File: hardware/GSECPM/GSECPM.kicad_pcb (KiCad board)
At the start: 2 copper layers, 167.8 x 110.5 mm, 67 parts, among them J1 N2-Bottle PT, J10 Ignition E-Match, J11 QD E-Match, J12 Radio Module Connector, J13 Purge Servo, J14 Power Input, J15 Internal Cooling, J16 Nitrous Cooling, J17 Load Cell + Amp, J2 K-Bottle TC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

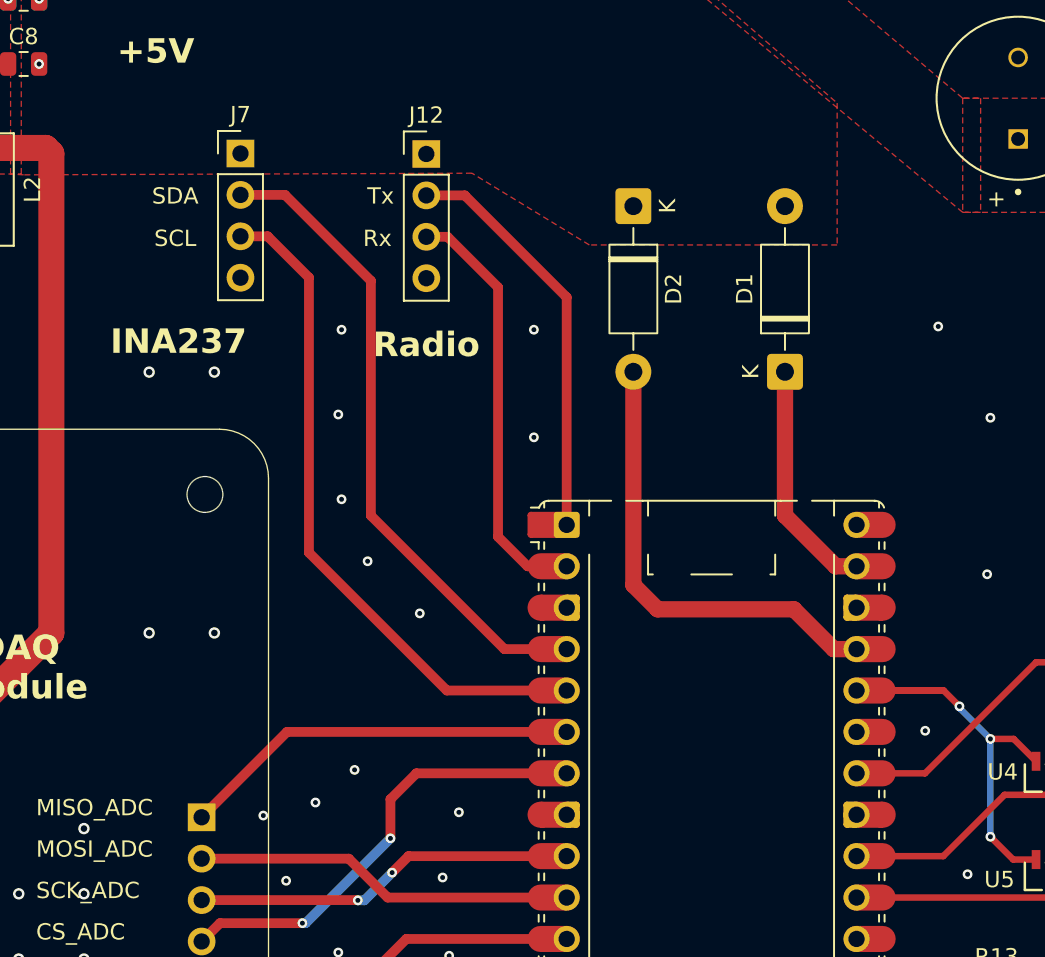
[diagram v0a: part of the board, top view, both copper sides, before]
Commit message: Swapped positions of radio and INA237 conns for optimized current loop. Swapped 9V LDO to a TI model that supports newer ceramic caps better than the original STM legacy LDO
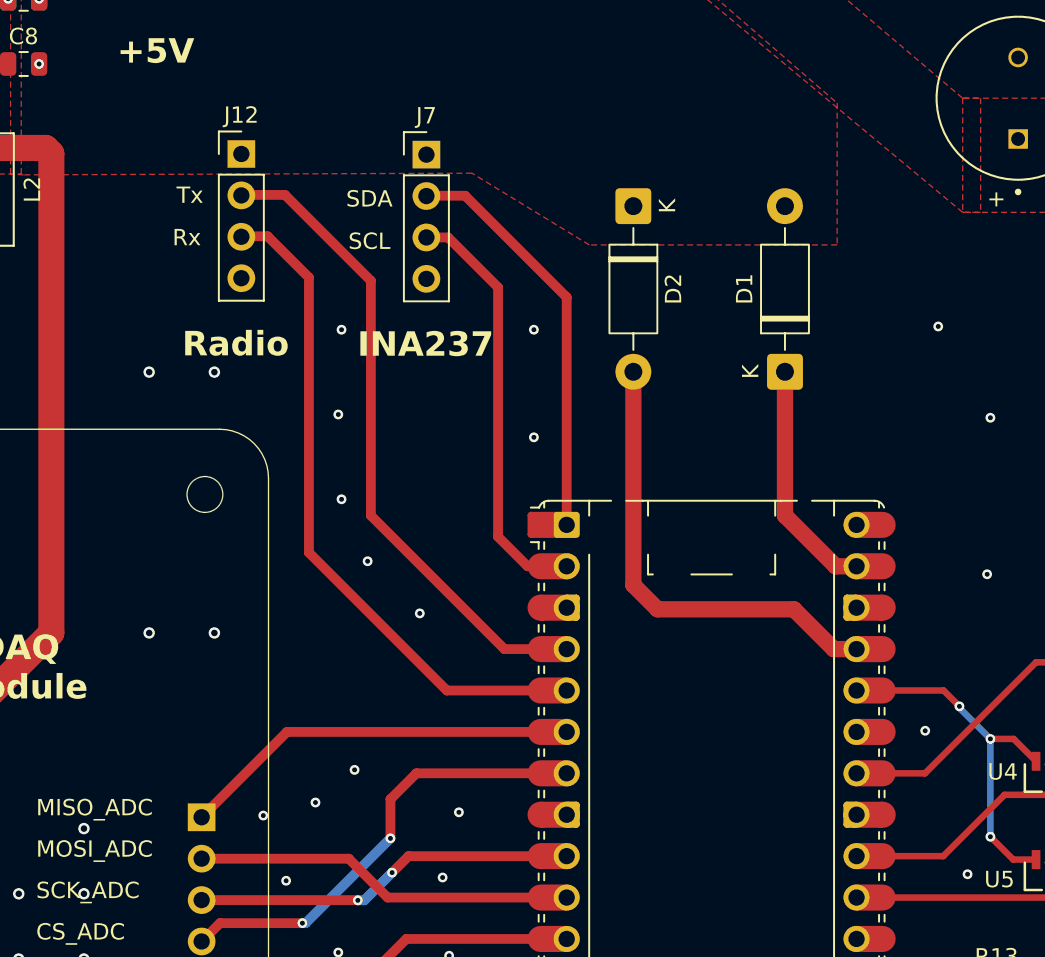
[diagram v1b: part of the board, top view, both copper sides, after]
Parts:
- U1: value L78M09CDT-TR -> UA78M09CKVURG3
- moved J7 11.4 mm to (139.7, 51.1)
- moved J12 11.3 mm to (128.3, 51.1)
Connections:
- A1 pad 1: /GPIO0 (Radio_UART_TX) -> /GPIO0_INA237 SDA
- A1 pad 2: /GPIO1 (Radio_UART_RX) -> /GPIO1_INA237 SCL
- A1 pad 4: /GPIO2_INA237 SDA -> /GPIO2 (Radio_UART_TX)
- A1 pad 5: /GPIO3_INA237 SCL -> /GPIO3 (Radio_UART_RX)
- J12 pad 2: /GPIO0 (Radio_UART_TX) -> /GPIO2 (Radio_UART_TX)
- J12 pad 3: /GPIO1 (Radio_UART_RX) -> /GPIO3 (Radio_UART_RX)
- J7 pad 2: /GPIO2_INA237 SDA -> /GPIO0_INA237 SDA
- J7 pad 3: /GPIO3_INA237 SCL -> /GPIO1_INA237 SCL
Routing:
- net /GPIO3_INA237 SCL: track 41.4 -> 0.00 mm
- net /GPIO3 (Radio_UART_RX): track 0.00 -> 41.4 mm
- net /GPIO2 (Radio_UART_TX): track 0.00 -> 40.8 mm
- net /GPIO2_INA237 SDA: track 40.0 -> 0.00 mm
- net /GPIO1_INA237 SCL: track 0.00 -> 25.9 mm
- net /GPIO1 (Radio_UART_RX): track 25.9 -> 0.00 mm
- net /GPIO0 (Radio_UART_TX): track 25.2 -> 0.00 mm
- net /GPIO0_INA237 SDA: track 0.00 -> 25.2 mm
- net +3.3V: track 26.8 -> 22.2 mm
- net Net-(A1-GPIO27_ADC1): track 17.8 -> 18.6 mm

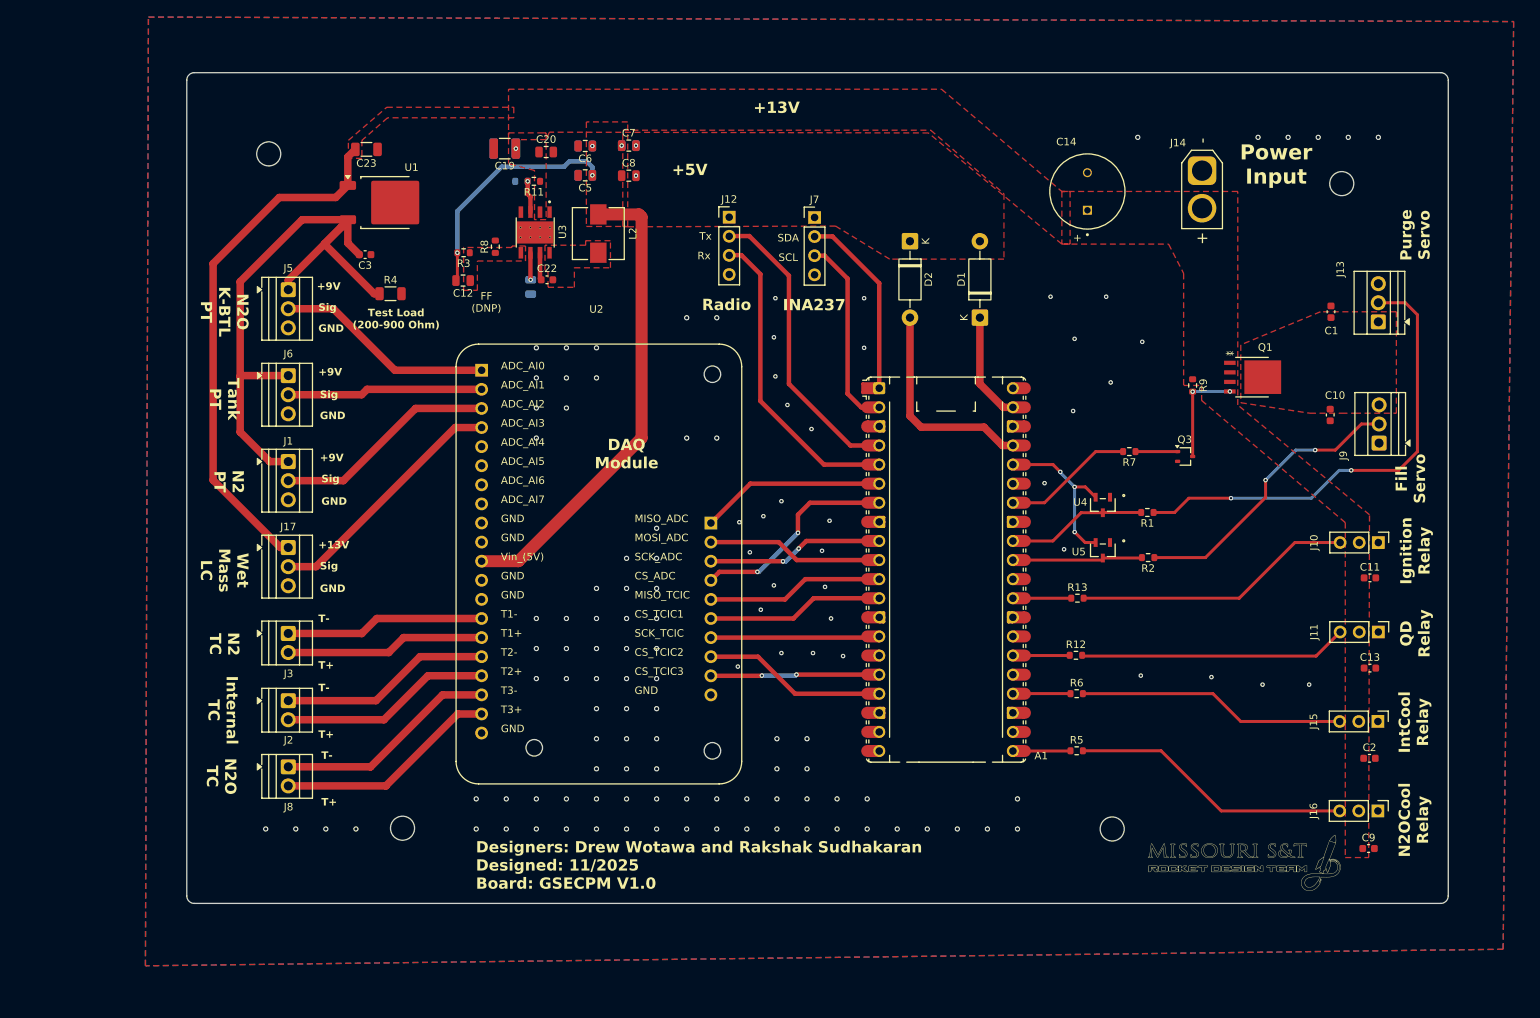
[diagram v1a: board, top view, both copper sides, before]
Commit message: Made all buck components on front layer
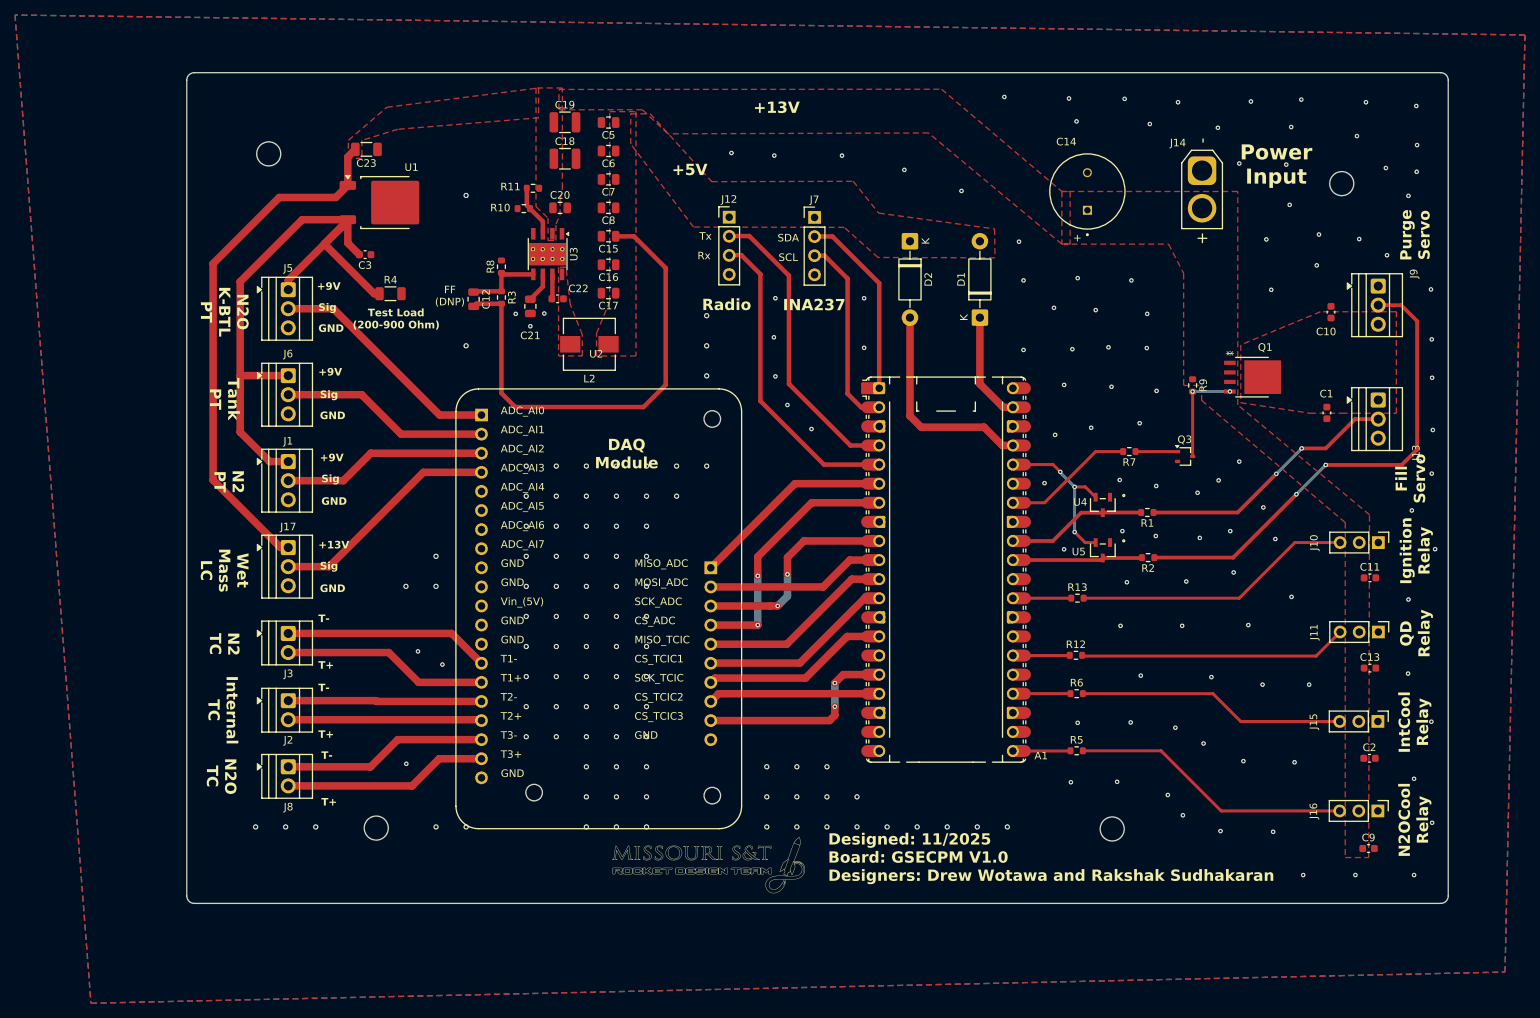
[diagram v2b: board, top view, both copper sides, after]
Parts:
- C15, C16, C17, C18, C21, R10: moved to F.Cu
- U3: footprint LMR33640ADDAR:VREG_LM5017MR_NOPB -> Package_SO:Texas_HSOP-8-1EP_3.9x4.9mm_P1.27mm_ThermalVias
- moved G*** 71.3 mm to (125.5, 137.3)
- moved J9 20.9 mm to (214.6, 60.3), turned to -90 degrees
- moved C17 19.8 mm to (112.2, 61.2), turned to 180 degrees
- moved C16 16.1 mm to (112.2, 57.4)
- moved L2 14.8 mm to (109.7, 68.0), turned to 0 degrees
- moved C10 13.7 mm to (208.3, 63.7), turned to 90 degrees
- moved C1 13.5 mm to (207.8, 77.1), turned to 90 degrees
- moved J13 10.4 mm to (214.6, 75.4), turned to -90 degrees
- moved C19 8.74 mm to (106.5, 38.5), turned to 0 degrees
- moved C15 8.69 mm to (112.2, 53.6)
- moved C18 8.12 mm to (106.5, 43.3), turned to 0 degrees
- moved R3 7.80 mm to (98.0, 61.8), turned to -90 degrees
- moved C5 7.67 mm to (112.2, 38.5)
- moved C20 7.66 mm to (105.8, 49.9)
- moved U2 5.96 mm to (110.6, 69.8)
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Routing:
- net +5V: track 94.8 -> 63.5 mm, vias 4 -> 0
- net /GPIO27 (Purge Servo): track 62.5 -> 35.0 mm
- net /GPIO26 (Fill Servo): track 38.6 -> 64.0 mm
- net /BuckConverter/FB: track 0.00 -> 10.5 mm
- net /GPIO5 (CS_ADC): track 28.1 -> 34.5 mm
- net /GPIO6 (SCK_ADC): track 23.5 -> 29.0 mm
- net /GPIO12 (CS_N2O): track 22.5 -> 27.5 mm
- net /GPIO10 (SCK_TCIC): track 22.5 -> 25.2 mm
- net Net-(U3-EN): track 4.25 -> 6.94 mm, vias 1 -> 0
- net /T+ (N2O): track 29.7 -> 27.2 mm
- net /T- (N2O): track 29.7 -> 27.2 mm
- net /GPIO9 (CS_N2): track 23.5 -> 26.0 mm
- net /ADC_AI3: track 33.4 -> 30.9 mm
- net /GPIO4 (MISO_ADC): track 24.6 -> 27.0 mm
- net /GPIO8 (MISO_TCIC): track 23.5 -> 26.0 mm
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- removed copper zone on F.Cu, net /BuckConverter/FB
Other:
- board text added: "Designed: 11/2025 Board: GSECPM V1.0 Designers: Drew Wotawa and Rakshak Sudhakaran"
- board text added: "{ "ViaStitching": "0.2", "stitch_zone_0": { "HSpacing": "1", "VSpacing": "1", "HOffset": "0", "VOffset": "0", "Clearance": "1", "Randomize": false } }"
- board text added: "{ "ViaStitching": "0.2", "stitch_zone_0": { "HSpacing": "4", "VSpacing": "4", "HOffset": "0", "VOffset": "0", "Clearance": "0", "Randomize": false } }"
- board text removed: "Designers: Drew Wotawa and Rakshak Sudhakaran Designed: 11/2025 Board: GSECPM V1.0"

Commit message: Better buck converter positioning with inductor further from analog signals. Improved via stitching and fixed split ground planes somewhat except for Manhattans
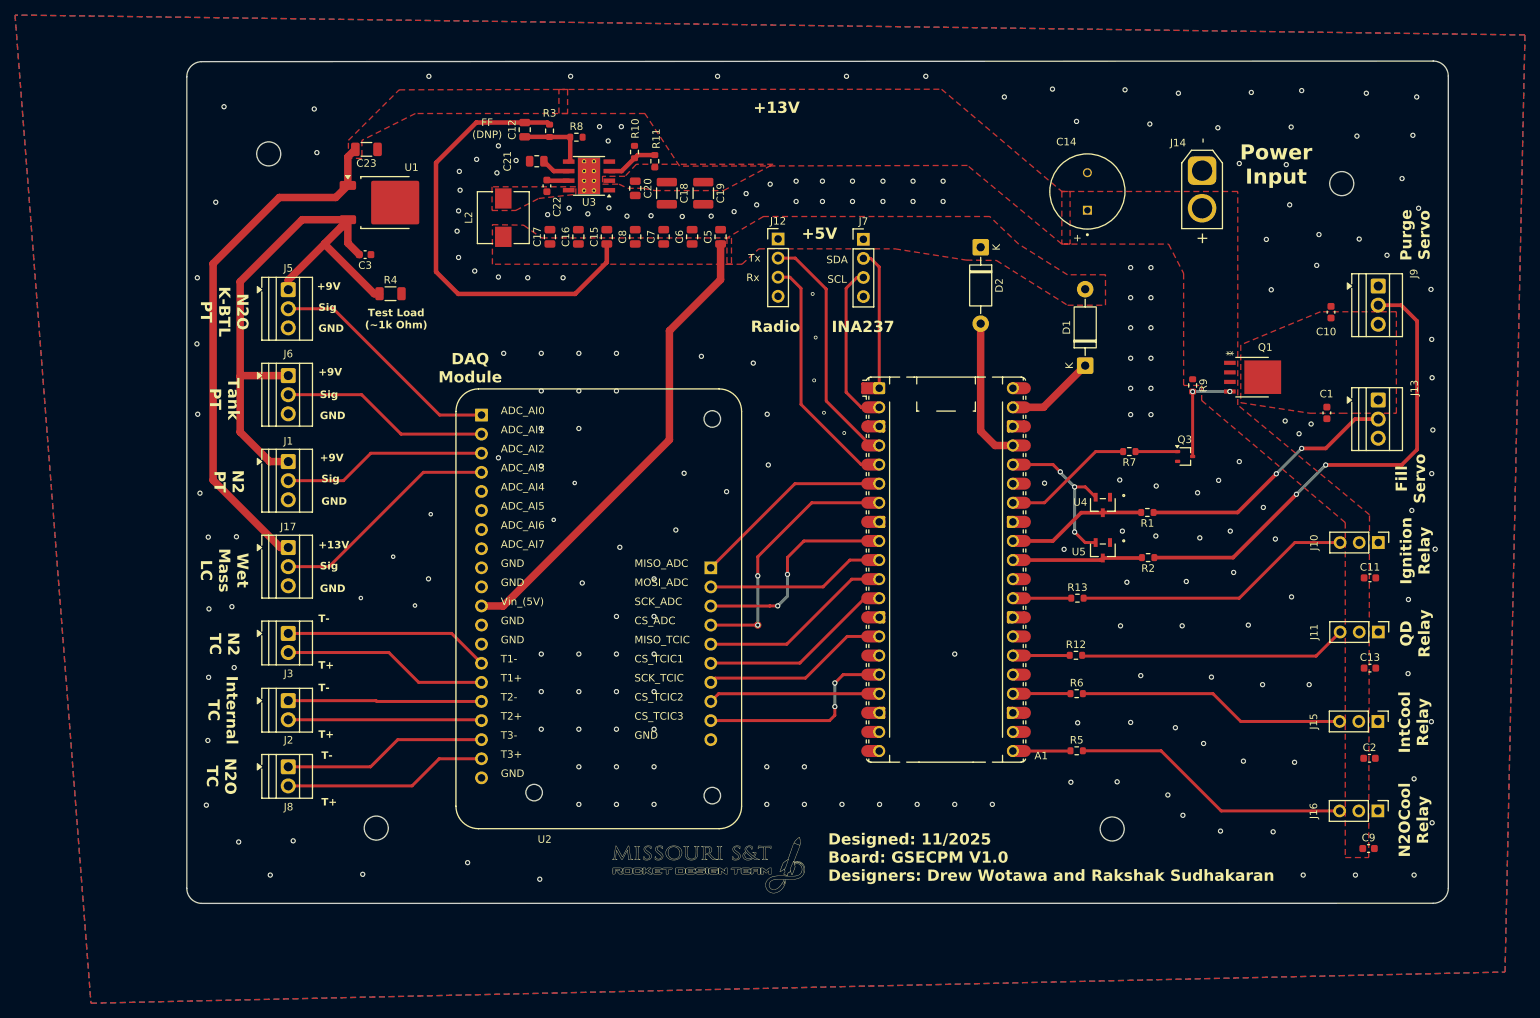
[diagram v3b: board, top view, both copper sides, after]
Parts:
- moved C12 23.6 mm to (101.1, 39.5), turned to 90 degrees
- moved R3 23.1 mm to (104.4, 39.6), turned to 90 degrees
- moved C5 21.3 mm to (127.2, 53.7), turned to 90 degrees
- moved C19 20.7 mm to (124.8, 47.9), turned to -90 degrees
- moved L2 20.4 mm to (98.2, 51.1), turned to -90 degrees
- moved R8 19.9 mm to (108.0, 40.5), turned to 0 degrees
- moved C21 19.3 mm to (102.7, 43.6), turned to 180 degrees
- moved R11 16.6 mm to (118.4, 43.6), turned to 90 degrees
- moved R10 16.5 mm to (115.7, 42.4), turned to -90 degrees
- moved C6 15.9 mm to (123.4, 53.7), turned to 90 degrees
- moved D1 15.4 mm to (175.7, 70.8)
- moved C22 15.1 mm to (104.0, 46.9), turned to -90 degrees
- moved C18 14.3 mm to (120.0, 47.9), turned to -90 degrees
- moved U3 11.8 mm to (109.7, 45.6), turned to 180 degrees
- moved C17 10.8 mm to (104.5, 53.7), turned to 90 degrees
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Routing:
- net +5V: track 63.5 -> 123.1 mm
- net Net-(A1-3V3_EN): track 28.4 -> 19.4 mm
- net /GPIO3 (Radio_UART_RX): track 41.4 -> 32.8 mm
- net /GPIO2 (Radio_UART_TX): track 40.8 -> 33.3 mm
- net /GPIO0_INA237 SDA: track 25.2 -> 18.7 mm
- net /GPIO1_INA237 SCL: track 25.9 -> 22.0 mm
- net Net-(A1-VSYS): track 14.5 -> 11.9 mm
- net /BuckConverter/FB: track 10.5 -> 9.40 mm
- net GND: vias 203 -> 221
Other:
- board size 167.8 x 110.5 mm -> 167.8 x 112 mm
- board text added: "Test Load (~1k Ohm)"
- board text added: "{ "ViaStitching": "0.2", "stitch_zone_0": { "HSpacing": "5", "VSpacing": "5", "HOffset": "0", "VOffset": "0", "Clearance": "4", "Randomize": false } }"
- board text removed: "Test Load (200-900 Ohm)"

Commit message: Finished PCBs with production files
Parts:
- removed C23: 0.33u, Capacitor_SMD:C_1206_3216Metric
- added C4: 10u, Capacitor_SMD:C_1210_3225Metric, F.Cu at (80.1, 41.8)
- C3: value 100n -> 10u; footprint Capacitor_SMD:C_0603_1608Metric -> Capacitor_SMD:C_1210_3225Metric
- Q1: value BUK6Y33-60PX -> PSMP033-60YEX
- U1: value UA78M09CKVURG3 -> BD90C0AFP-CE2
- moved C3 2.86 mm to (82.7, 55.9)
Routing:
- net +9V: track 83.3 -> 87.1 mm
